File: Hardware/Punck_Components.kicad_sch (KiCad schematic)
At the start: 114 parts, among them J1 Conn_01x12_Female, J2 Conn_01x12_Female, J3 Conn_01x12_Female, J4 Conn_01x12_Female, J5 Debug_Header, J6 SWD_Header, J7 Eurorack_10_pin_power, Q1 MMBT3904, Q2 MMBT3904, Q3 MMBT3904, Q4 MMBT3904, Q5 MMBT3904, Q6 MMBT3904, Q7 MMBT3904, U1 TL074, U2 STM32H743ZITx, U3 W25Q128JVS, U4 PCM5100APW, U5 W25Q128JVS, U6 TPS561201, U7 LD1117-3.3-4Tab, Y1 8MHz 20pF

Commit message: Fixes to copper pour on L2 for v1 production
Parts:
- C38, C39, C40: footprint Resistor_SMD:R_0805_2012Metric -> Capacitor_SMD:C_0805_2012Metric
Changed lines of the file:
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@@
     (property "Reference" "C39" (id 0) (at 105.41 259.08 0))
     (property "Value" "10uF" (id 1) (at 105.41 264.16 0))
-    (property "Footprint" "Resistor_SMD:R_0805_2012Metric" (id 2) (at 107.95 261.62 0)
+    (property "Footprint" "Capacitor_SMD:C_0805_2012Metric" (id 2) (at 107.95 261.62 0)
       (effects (font (size 1.27 1.27)) hide)
     )
@@
     (property "Reference" "C40" (id 0) (at 113.03 259.08 0))
     (property "Value" "10uF" (id 1) (at 113.03 264.16 0))
-    (property "Footprint" "Resistor_SMD:R_0805_2012Metric" (id 2) (at 115.57 261.62 0)
+    (property "Footprint" "Capacitor_SMD:C_0805_2012Metric" (id 2) (at 115.57 261.62 0)
       (effects (font (size 1.27 1.27)) hide)
     )
@@
     (property "Reference" "C38" (id 0) (at 152.4 256.54 0))
     (property "Value" "100nF" (id 1) (at 149.86 259.08 0))
-    (property "Footprint" "Resistor_SMD:R_0805_2012Metric" (id 2) (at 149.86 255.27 0)
+    (property "Footprint" "Capacitor_SMD:C_0805_2012Metric" (id 2) (at 149.86 255.27 0)
       (effects (font (size 1.27 1.27)) hide)
     )
@@
     )
     (path "/d2a7b285-1032-46ff-a18a-afc781d06f96"
-      (reference "C38") (unit 1) (value "100nF") (footprint "Resistor_SMD:R_0805_2012Metric")
+      (reference "C38") (unit 1) (value "100nF") (footprint "Capacitor_SMD:C_0805_2012Metric")
     )
     (path "/10fcd67d-3f8c-4430-8de1-728b6d3c2ed4"
-      (reference "C39") (unit 1) (value "10uF") (footprint "Resistor_SMD:R_0805_2012Metric")
+      (reference "C39") (unit 1) (value "10uF") (footprint "Capacitor_SMD:C_0805_2012Metric")
     )
     (path "/5dfde6b0-58e2-4528-a7e0-dffdbc1a442e"
-      (reference "C40") (unit 1) (value "10uF") (footprint "Resistor_SMD:R_0805_2012Metric")
+      (reference "C40") (unit 1) (value "10uF") (footprint "Capacitor_SMD:C_0805_2012Metric")
     )
     (path "/00000000-0000-0000-0000-00005f1d3990"

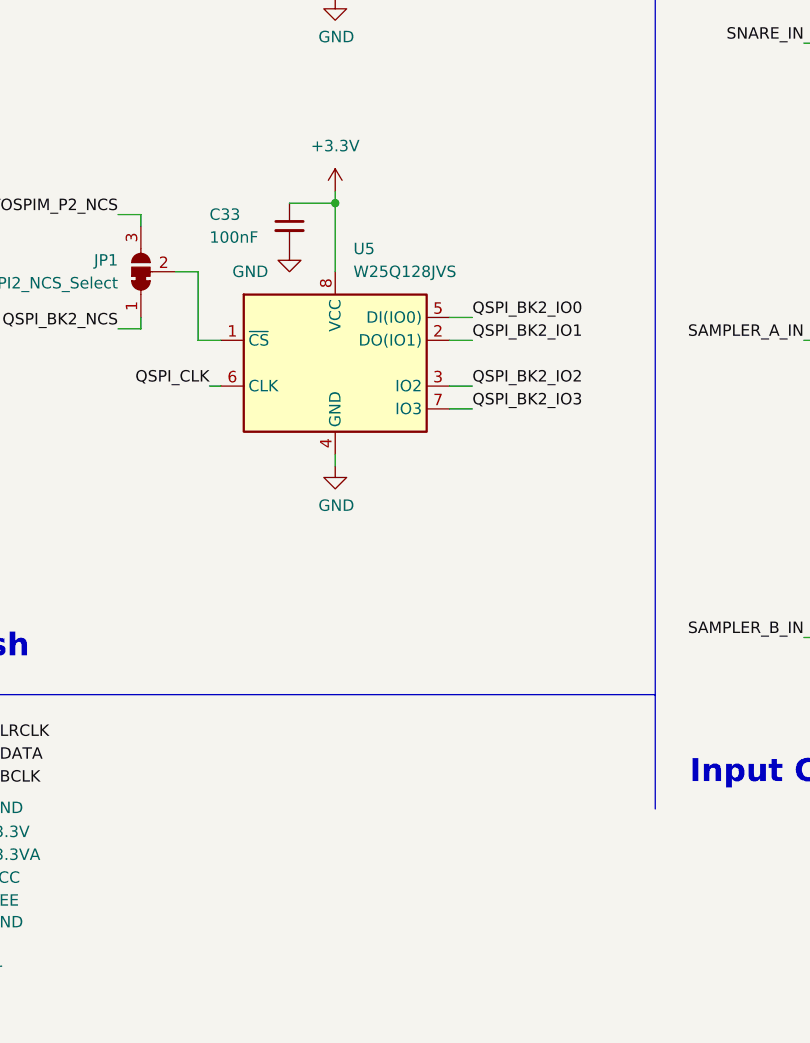
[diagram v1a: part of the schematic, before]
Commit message: Started altering project to bring up v1 hardware
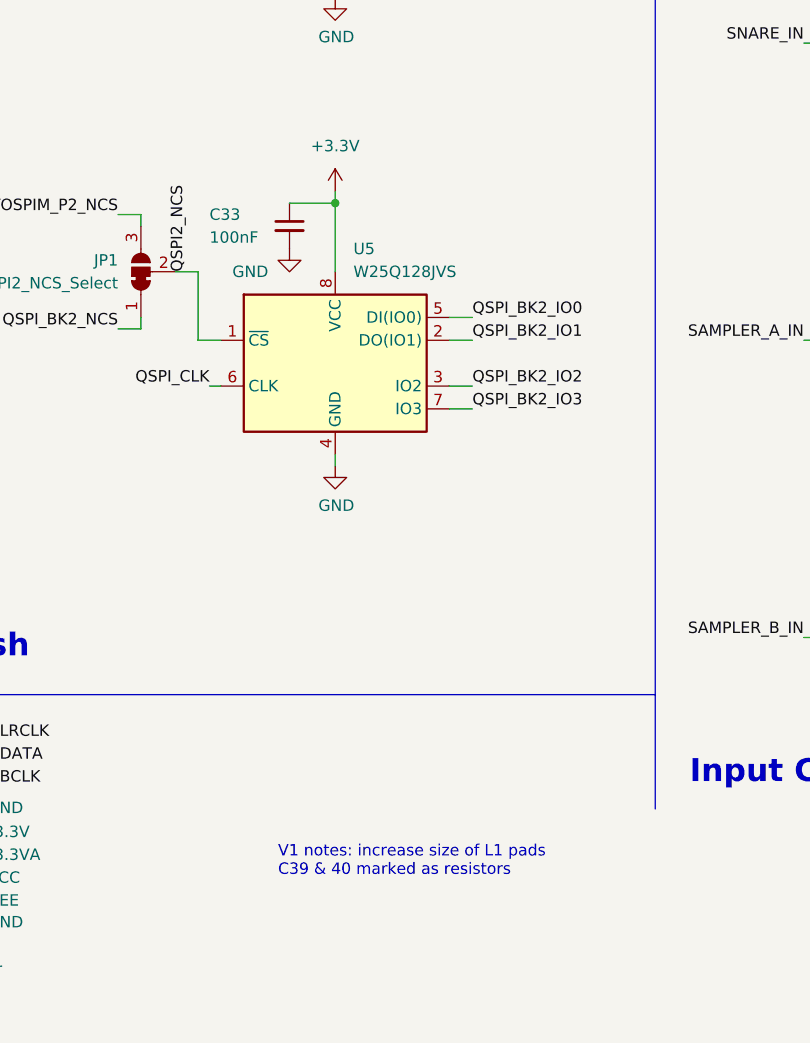
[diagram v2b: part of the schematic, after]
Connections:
- net QSPI2_NCS: now reaches JP1.2 (C), U5.1 (~{CS})
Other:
- note added: "V1 notes: increase size of L1 pads C39 & 40 marked as resistors"
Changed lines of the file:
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@@
     (effects (font (size 2.54 2.54) (thickness 0.508) bold) (justify left bottom))
+  )
+  (text "V1 notes: increase size of L1 pads\nC39 & 40 marked as resistors"
+    (at 308.61 260.35 0)
+    (effects (font (size 1.27 1.27)) (justify left bottom))
   )
   (text "Power" (at 15.24 281.94 0)
@@
     (effects (font (size 1.27 1.27)) (justify left bottom))
   )
+  (label "QSPI2_NCS" (at 298.45 193.04 90)
+    (effects (font (size 1.27 1.27)) (justify left bottom))
+  )

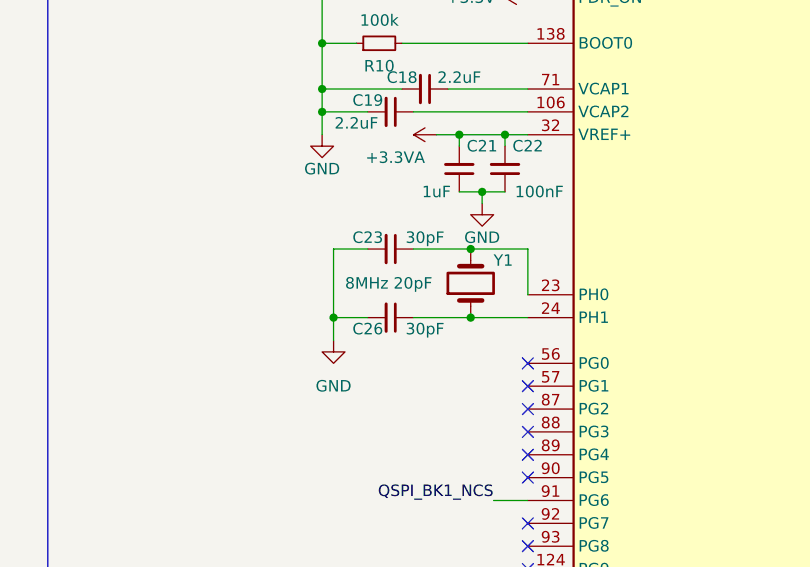
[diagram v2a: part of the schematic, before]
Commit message: Added tempo clock out functionality
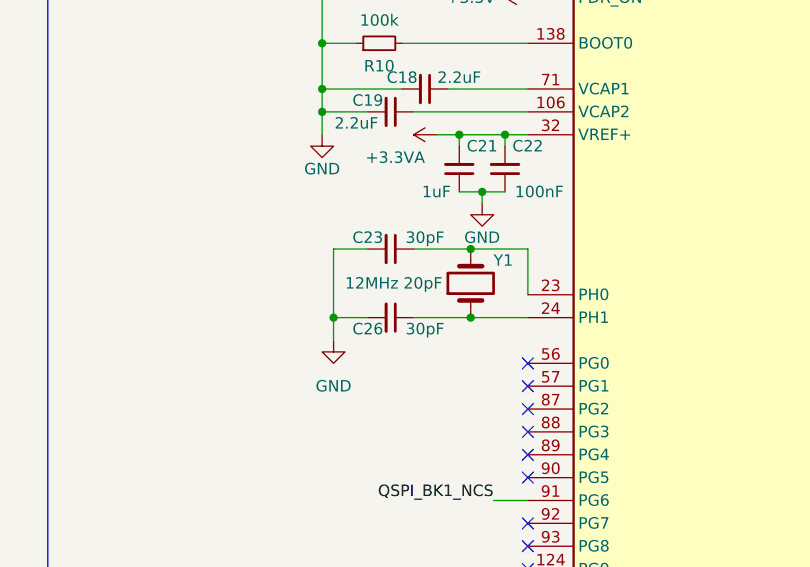
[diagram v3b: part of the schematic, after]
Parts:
- Y1: value 8MHz 20pF -> 12MHz 20pF
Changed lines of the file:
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@@
       (effects (font (size 1.27 1.27)) (justify right))
     )
-    (property "Value" "8MHz 20pF" (id 1) (at 24.13 83.82 90)
+    (property "Value" "12MHz 20pF" (id 1) (at 24.13 83.82 90)
       (effects (font (size 1.27 1.27)) (justify right))
     )
@@
     )
     (path "/00000000-0000-0000-0000-00005f020654"
-      (reference "Y1") (unit 1) (value "8MHz 20pF") (footprint "Crystal:Crystal_SMD_5032-2Pin_5.0x3.2mm")
+      (reference "Y1") (unit 1) (value "12MHz 20pF") (footprint "Crystal:Crystal_SMD_5032-2Pin_5.0x3.2mm")
     )
   )
